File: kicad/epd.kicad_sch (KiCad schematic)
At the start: 26 parts, among them Q401 SI1308EDL

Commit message: finish management schematic, ready for PCB
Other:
- note added: "DEFAULT 1"
- note removed: "1 IS DEFAULT"
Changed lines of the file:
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@@
 		)
 	)
-	(text "1 IS DEFAULT"
+	(text "DEFAULT 1"
 		(exclude_from_sim no)
 		(at 93.98 162.306 0)
@@
 		)
 	)
-	(text "1 IS DEFAULT"
+	(text "DEFAULT 1"
 		(exclude_from_sim no)
 		(at 141.732 152.146 0)

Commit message: Revision 2: Fix MOSFET pins and various changes
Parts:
- removed Q401: SI1308EDL, Package_TO_SOT_SMD:SOT-323_SC-70_Handsoldering, symbol Simulation_SPICE:NMOS
- added Q401: Si1308EDL, Package_TO_SOT_SMD:SOT-323_SC-70, symbol Transistor_FET:Si1308EDL
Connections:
- net GDR: now also Q401.1 (G)
- net RESE: now also Q401.2 (S)
- net at C403.1, D401.2 (A), L401.1: now also Q401.3 (D)
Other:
- note added: "Horribly annoying issue in previous revision where NMOS pins were in the wrong order"
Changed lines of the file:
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@@
+		)
+	)
+	(text "Horribly annoying issue in previous\nrevision where NMOS pins were\nin the wrong order"
+		(exclude_from_sim no)
+		(at 96.266 82.804 0)
+		(effects
+			(font
+				(size 1.27 1.27)
+			)
 		)
 	)
@@
 			)
 			(justify left)
+		)
+	)
+	(symbol
+		(lib_id "Transistor_FET:Si1308EDL")
+		(at 93.98 63.5 0)
+		(unit 1)
+		(exclude_from_sim no)
+		(in_bom yes)
+		(on_board yes)
+		(dnp no)
+		(fields_autoplaced yes)
+		(property "Reference" "Q401"
+			(at 100.33 62.2299 0)
+			(effects
+				(font
+					(size 1.27 1.27)
+				)
+				(justify left)
+			)
+		)
+		(property "Value" "Si1308EDL"
+			(at 100.33 64.7699 0)
+			(effects
+				(font
+					(size 1.27 1.27)
+				)
+				(justify left)
+			)
+		)
+		(property "Footprint" "Package_TO_SOT_SMD:SOT-323_SC-70"
+			(at 99.06 65.405 0)
+			(effects
+				(font
+					(size 1.27 1.27)
+					(italic yes)
+				)
+				(justify left)
+				(hide yes)
+			)
+		)
+		(property "Datasheet" "https://www.vishay.com/docs/63399/si1308edl.pdf"
+			(at 99.06 67.31 0)
+			(effects
+				(font
+					(size 1.27 1.27)
+				)
+				(justify left)
+				(hide yes)
+			)
+		)
+		(property "Description" "30V Vds, 1.4A Id, N-Channel MOSFET, SC-70"
+			(at 93.98 63.5 0)
+			(effects
+				(font
+					(size 1.27 1.27)
+				)
+				(hide yes)
+			)
+		)
+		(pin "3"
+		)
+		(pin "2"
+		)
+		(pin "1"
+		)
+		(instances
+			(project "kicad"
+				(path "/97e37379-fec6-4f0d-82d9-4ea53516bb02/0b88743c-b183-4be0-afee-bdc67a5fc676"
+					(reference "Q401")
+					(unit 1)
+				)
+			)
 		)
 	)
@@
 					(unit 1)
 				)
-			)
-		)
-	)
-	(symbol
-		(lib_id "Simulation_SPICE:NMOS")
-		(at 93.98 63.5 0)
-		(unit 1)
-		(exclude_from_sim no)
-		(in_bom yes)
-		(on_board yes)
-		(dnp no)
-		(property "Reference" "Q401"
-			(at 100.076 62.484 0)
-			(effects
-				(font
-					(size 1.27 1.27)
-				)
-				(justify left)
-			)
-		)
-		(property "Value" "SI1308EDL"
-			(at 98.552 64.77 0)
-			(effects
-				(font
-					(size 1.27 1.27)
-				)
-				(justify left)
-			)
-		)
-		(property "Footprint" "Package_TO_SOT_SMD:SOT-323_SC-70_Handsoldering"
-			(at 99.06 60.96 0)
-			(effects
-				(font
-					(size 1.27 1.27)
-				)
-				(hide yes)
-			)
-		)
-		(property "Datasheet" "https://ngspice.sourceforge.io/docs/ngspice-html-manual/manual.xhtml#cha_MOSFETs"
-			(at 93.98 76.2 0)
-			(effects
-				(font
-					(size 1.27 1.27)
-				)
-				(hide yes)
-			)
-		)
-		(property "Description" "N-MOSFET transistor, drain/source/gate"
-			(at 93.98 63.5 0)
-			(effects
-				(font
-					(size 1.27 1.27)
-				)
-				(hide yes)
-			)
-		)
-		(property "Sim.Device" "NMOS"
-			(at 93.98 80.645 0)
-			(effects
-				(font
-					(size 1.27 1.27)
-				)
-				(hide yes)
-			)
-		)
-		(property "Sim.Type" "VDMOS"
-			(at 93.98 82.55 0)
-			(effects
-				(font
-					(size 1.27 1.27)
-				)
-				(hide yes)
-			)
-		)
-		(property "Sim.Pins" "1=D 2=G 3=S"
-			(at 93.98 78.74 0)
-			(effects
-				(font
-					(size 1.27 1.27)
-				)
-				(hide yes)
-			)
-		)
-		(property "JLC" "XXXXXX"
-			(at 93.98 63.5 0)
-			(effects
-				(font
-					(size 1.27 1.27)
-				)
-				(hide yes)
-			)
-		)
-		(property "LCSC" "XXXXXX"
-			(at 93.98 63.5 0)
-			(effects
-				(font
-					(size 1.27 1.27)
-				)
-				(hide yes)
-			)
-		)
-		(pin "1"
-		)
-		(pin "2"
-		)
-		(pin "3"
-		)
-		(instances
-			(project "kicad"
-				(path "/97e37379-fec6-4f0d-82d9-4ea53516bb02/0b88743c-b183-4be0-afee-bdc67a5fc676"
-					(reference "Q401")
-					(unit 1)
-				)

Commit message: Rev. 3: Fix issues
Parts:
- EPD_FPC401: footprint Raven:CONN24x1_FH34SRJ-24S-0.5SH50_HIR -> Raven:CONN_F3311A7H121024E200_AMP
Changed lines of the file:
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@@
 			)
 		)
-		(property "Footprint" "Raven:CONN24x1_FH34SRJ-24S-0.5SH50_HIR"
+		(property "Footprint" "Raven:CONN_F3311A7H121024E200_AMP"
 			(at 196.85 80.01 0)
 			(effects

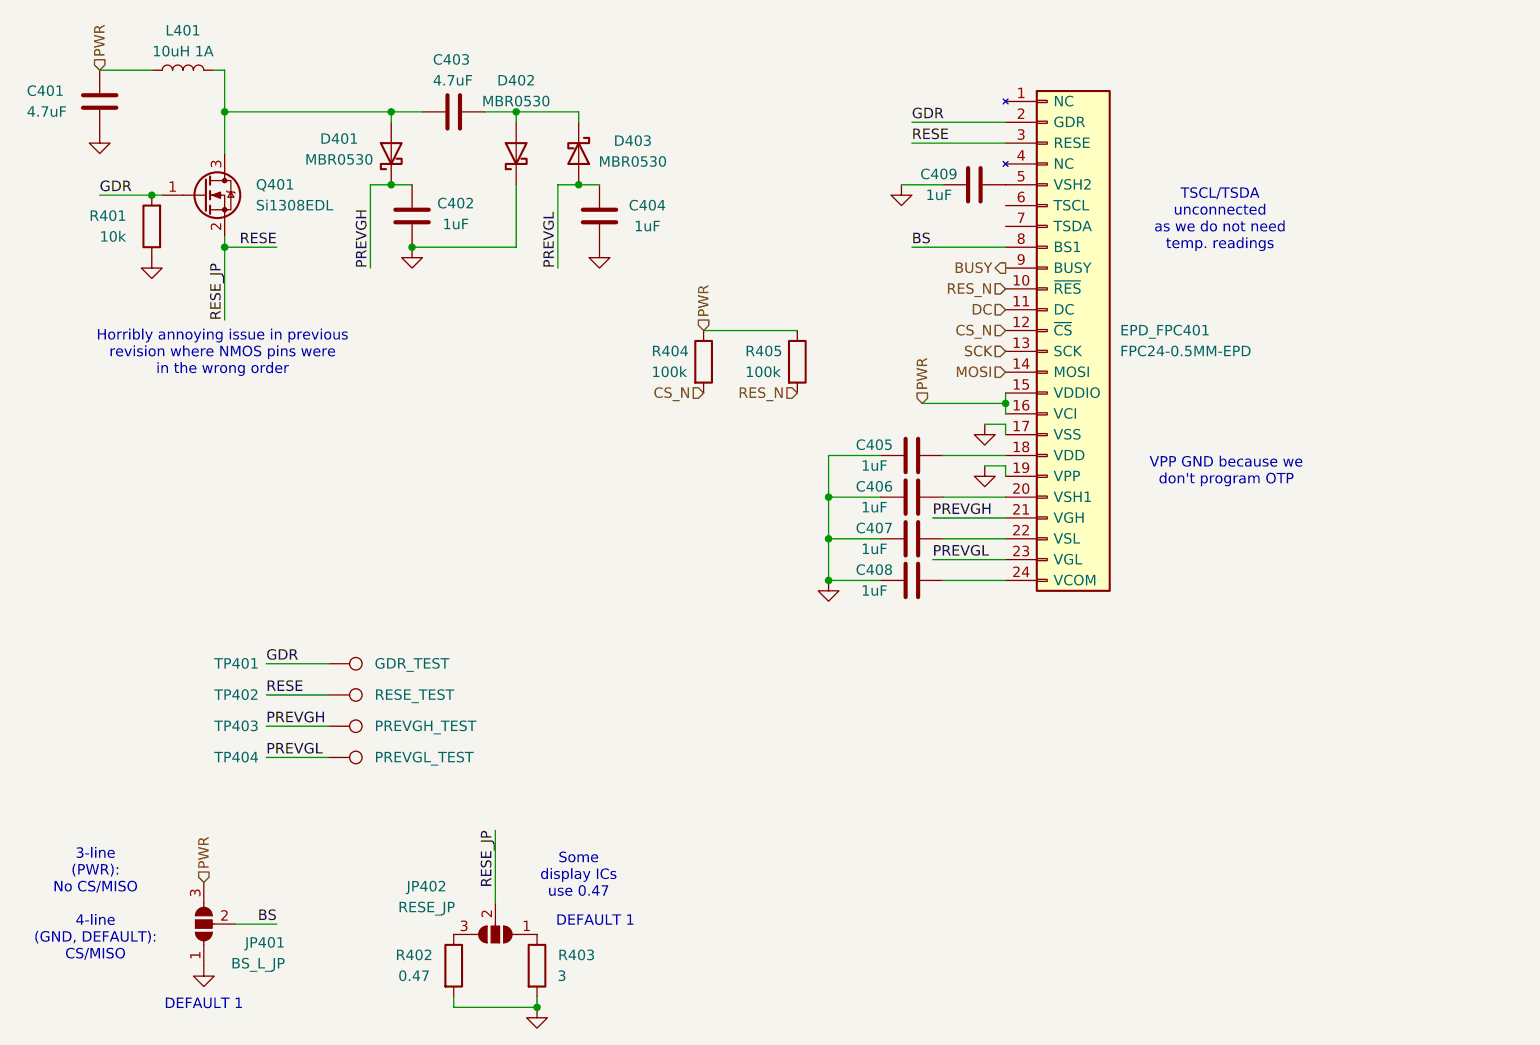
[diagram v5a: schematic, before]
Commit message: Microcontroller additions
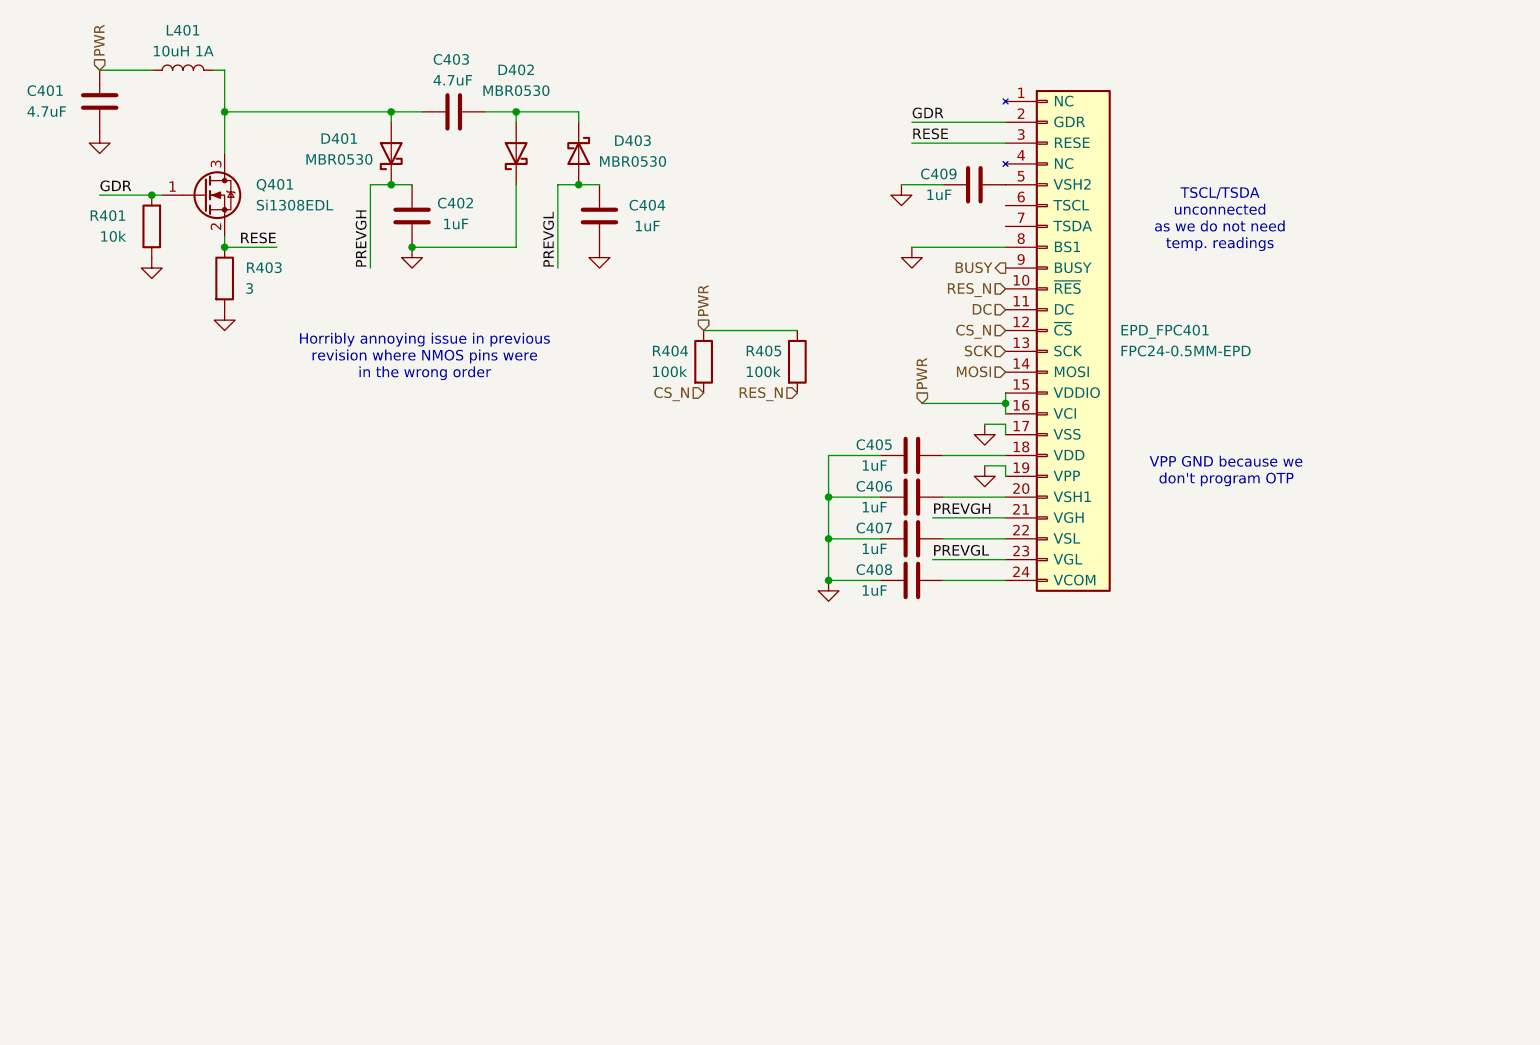
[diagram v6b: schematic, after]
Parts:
- removed JP401: BS_L_JP, Jumper:SolderJumper-3_P2.0mm_Open_TrianglePad1.0x1.5mm_NumberLabels, symbol Jumper:SolderJumper_3_Open
- removed JP402: RESE_JP, Jumper:SolderJumper-3_P2.0mm_Open_TrianglePad1.0x1.5mm_NumberLabels, symbol Jumper:SolderJumper_3_Open
- removed R402: 0.47, Resistor_SMD:R_0603_1608Metric_Pad0.98x0.95mm_HandSolder, symbol Device:R
- removed TP401: GDR_TEST, TestPoint:TestPoint_Pad_D1.5mm, symbol Connector:TestPoint
- removed TP402: RESE_TEST, TestPoint:TestPoint_Pad_D1.5mm, symbol Connector:TestPoint
- removed TP403: PREVGH_TEST, TestPoint:TestPoint_Pad_D1.5mm, symbol Connector:TestPoint
- removed TP404: PREVGL_TEST, TestPoint:TestPoint_Pad_D1.5mm, symbol Connector:TestPoint
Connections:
- net BS is gone; now on net GND: EPD_FPC401.8 (BS1)
- net RESE: now also R403.1
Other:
- note removed: "3-line (PWR): No CS/MISO 4-line (GND, DEFAULT): CS/MISO"
- note removed: "DEFAULT 1"
- note removed: "Some display ICs use 0.47"
- moved on the sheet: R403

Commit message: Unfinished switch additions and fixes
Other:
- note added: "Make sure NMOS pins are correct!! You can easily get this wrong"
- note removed: "Horribly annoying issue in previous revision where NMOS pins were in the wrong order"
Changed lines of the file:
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@@
 		)
 	)
-	(text "Horribly annoying issue in previous\nrevision where NMOS pins were\nin the wrong order"
+	(text "Make sure NMOS pins\nare correct!! You can\neasily get this wrong"
 		(exclude_from_sim no)
-		(at 120.904 83.312 0)
+		(at 111.506 84.328 0)
 		(effects
 			(font

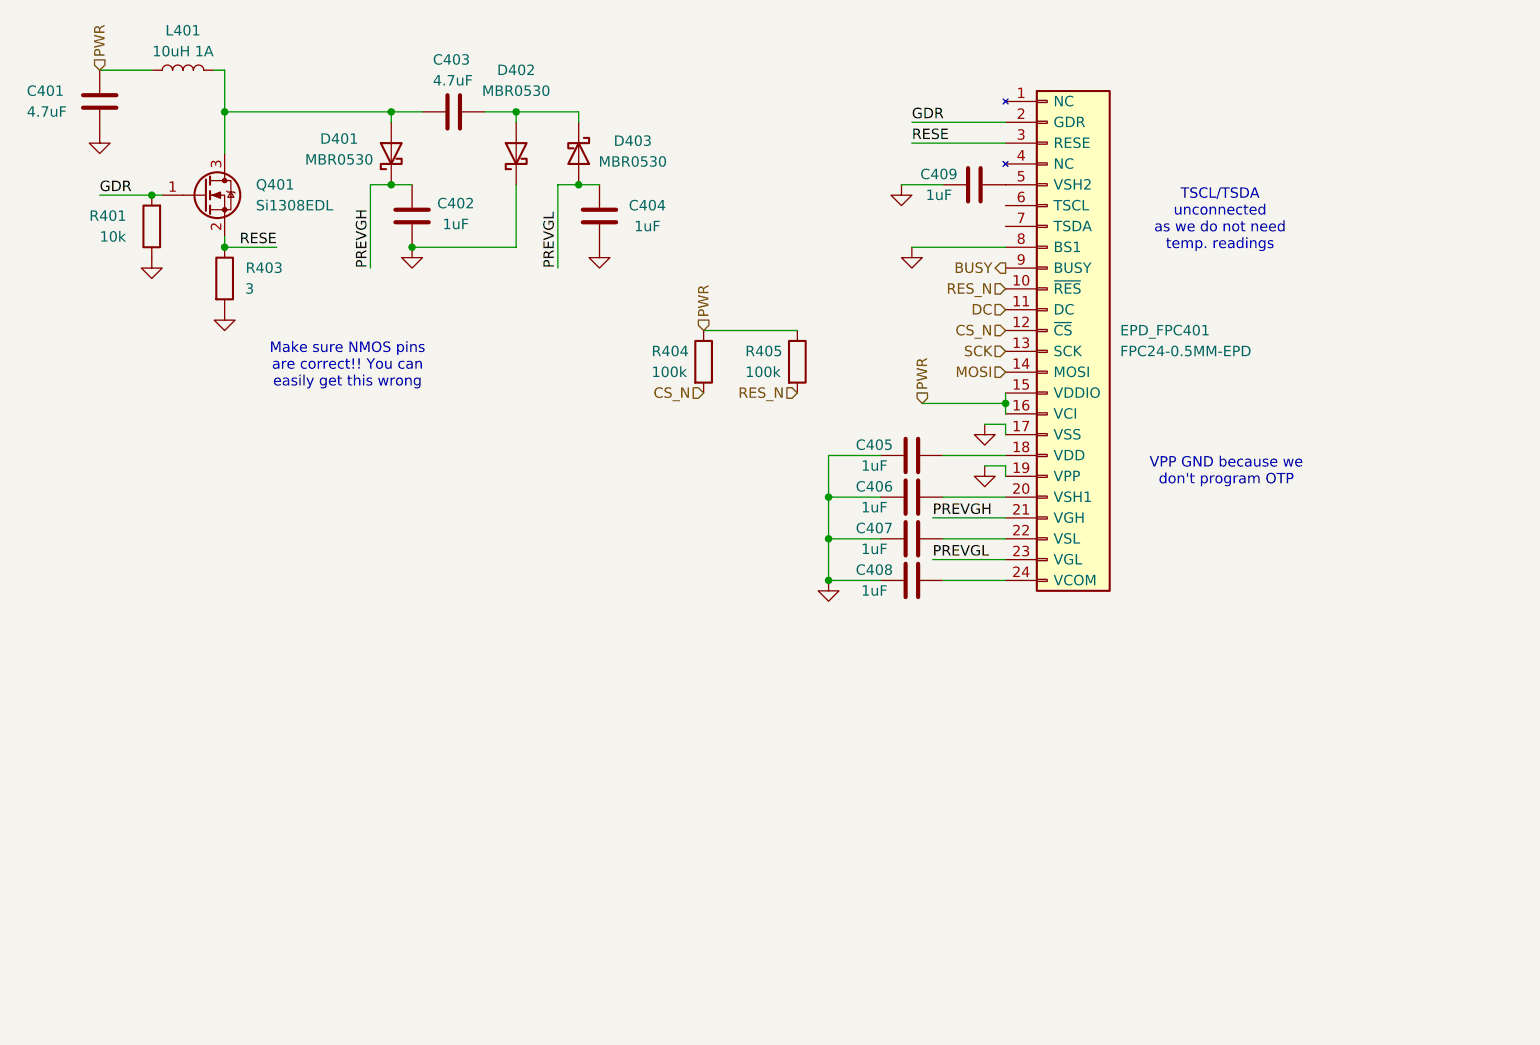
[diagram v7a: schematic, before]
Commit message: Small switch updates and fixes
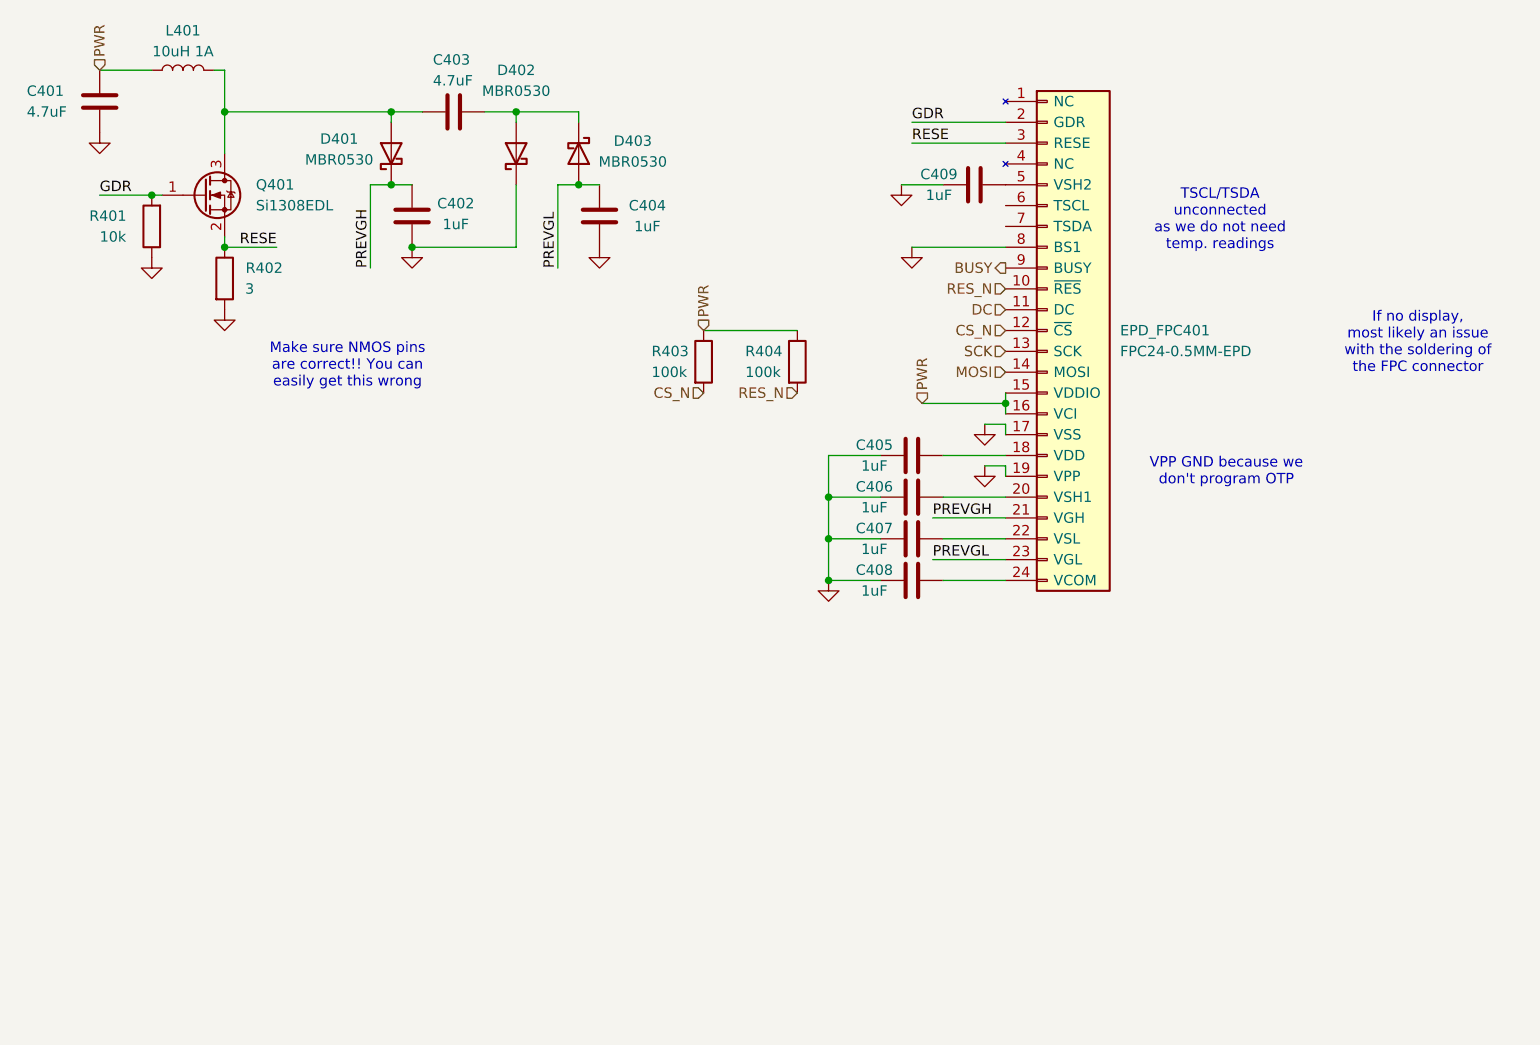
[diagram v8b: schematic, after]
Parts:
- renumbered R403 to R402, R404 to R403, R405 to R404
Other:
- note added: "If no display, most likely an issue with the soldering of the FPC connector"
